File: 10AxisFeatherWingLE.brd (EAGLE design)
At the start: 50.8 x 22.9 mm, 26 parts, among them J5 QWIIC, U1 LSM9DS1, U2 BME280

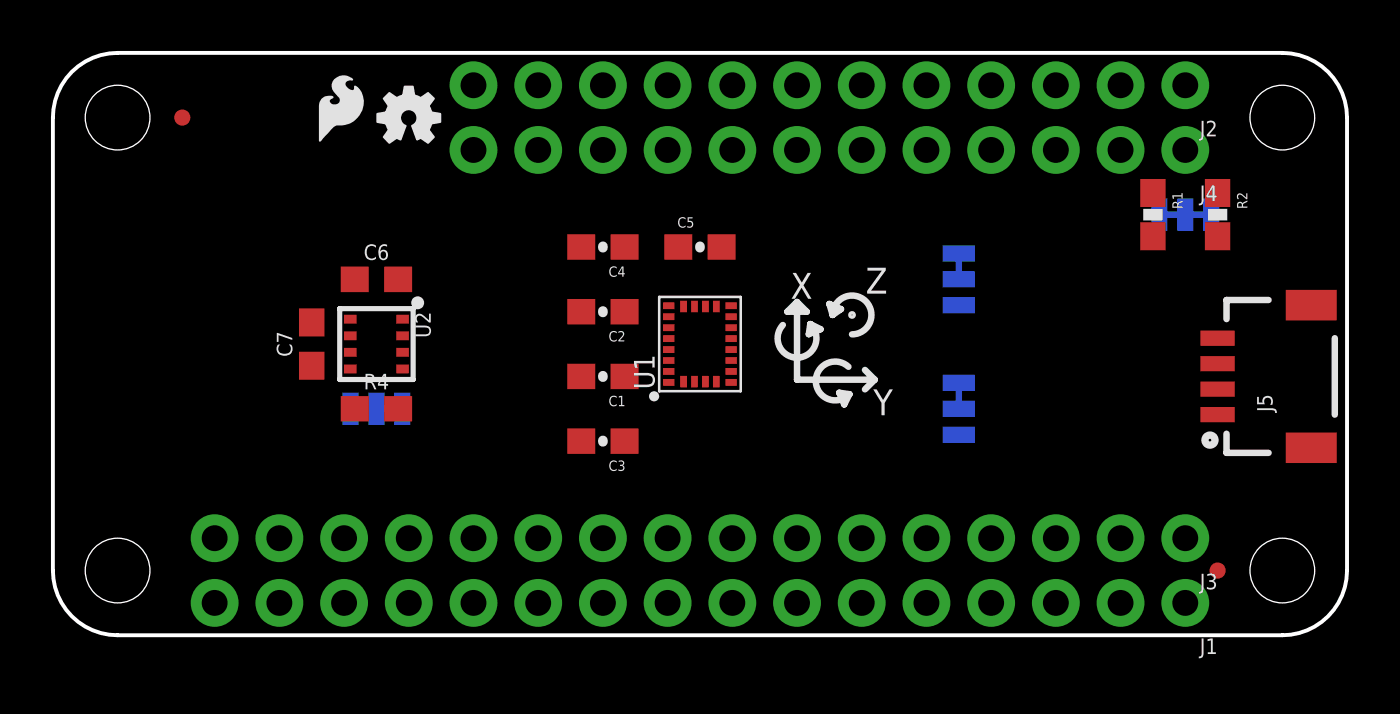
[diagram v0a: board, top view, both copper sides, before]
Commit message: Added traces
Added traces to board file.
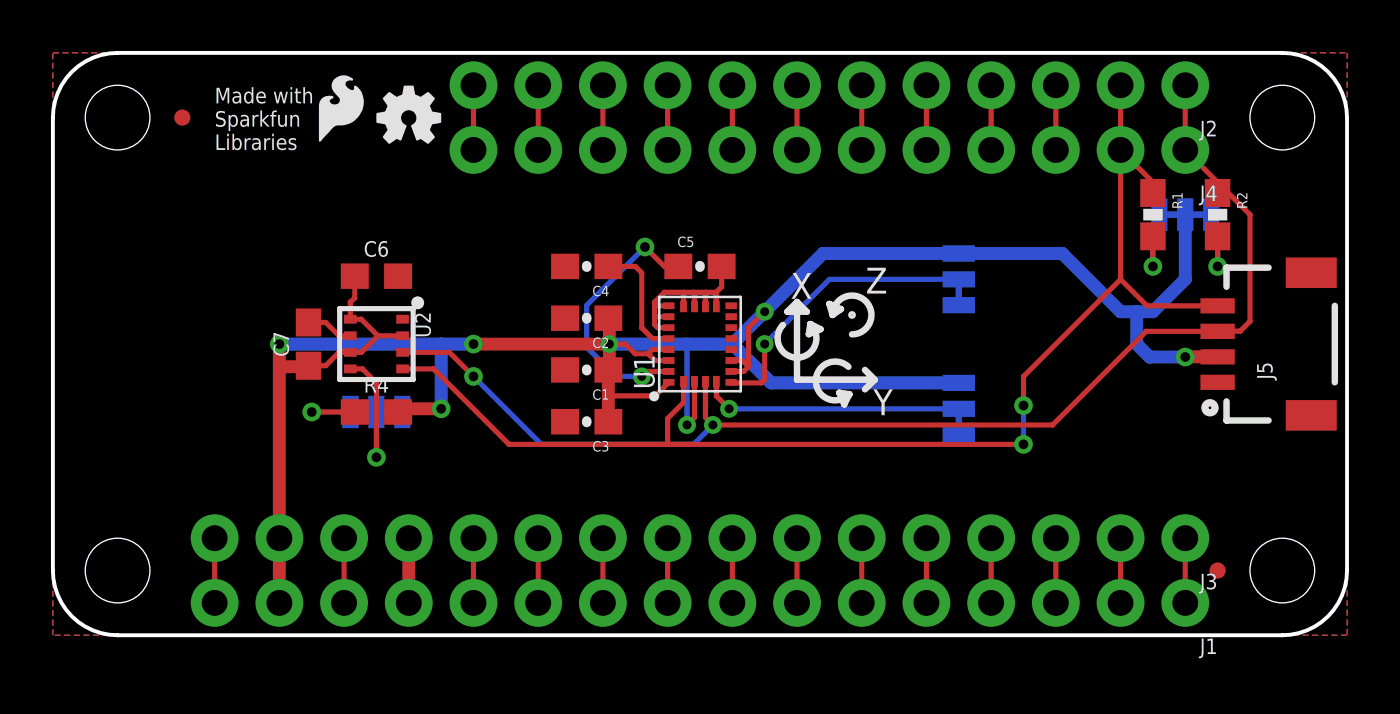
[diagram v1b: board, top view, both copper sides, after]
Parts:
- moved J5 1.27 mm to (45.7, 11.4)
- moved C4 0.99 mm to (21.0, 14.5)
- moved C3 0.99 mm to (21.0, 8.38)
- moved C5 0.76 mm to (25.4, 14.5)
- moved C1 0.68 mm to (21.0, 10.4)
- moved C2 0.68 mm to (21.0, 12.4)
- moved C7 0.13 mm to (10.0, 11.4)
- moved JP4 0.13 mm to (12.7, 8.76)
- moved R4 0.13 mm to (12.7, 8.76)
- moved C6 0.13 mm to (12.7, 14.1)
- turned JP2 to 270 degrees
- turned JP3 to 270 degrees
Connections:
- net SDO/ADR renamed SDO
- removed net SCK/SCL: U2.4
- removed net SDI/SDA: U2.3
- new net !RST: J1.16, J3.16
- new net A0: J1.12, J3.12
- new net A1: J1.11, J3.11
- new net A2: J1.10, J3.10
- new net A3: J1.9, J3.9
- new net A4: J1.8, J3.8
- new net A5: J1.7, J3.7
- new net AREF: J1.14, J3.14
- new net EN: J2.11, J4.11
- new net F0: J2.3, J4.3
- new net F1: J2.4, J4.4
- new net F2: J2.5, J4.5
- new net F3: J2.6, J4.6
- new net F4: J2.7, J4.7
- new net F5: J2.8, J4.8
- new net F6: J2.9, J4.9
- new net FREE: J1.1, J3.1
- new net MISO: J1.4, J3.4
- new net MOSI: J1.5, J3.5
- new net RX: J1.3, J3.3
- new net SCK: J1.6, J3.6
- new net TX: J1.2, J3.2
- new net VBAT: J2.12, J4.12
- new net VUSB: J2.10, J4.10
- net SCL: now also U2.4
- net SDA: now also U2.3
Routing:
- net VDD: track 0.00 -> 97.2 mm, vias 0 -> 7
- net SCL: track 0.00 -> 50.5 mm, vias 0 -> 2
- net SDA: track 0.00 -> 49.2 mm, vias 0 -> 2
- net GND: track 0.00 -> 13.0 mm
- net SDO_M: track 0.00 -> 11.0 mm, vias 0 -> 1
- net N$6: track 0.00 -> 10.3 mm, vias 0 -> 2
- net SDO_A/G: track 0.00 -> 9.88 mm, vias 0 -> 1
- net SDO: track 0.00 -> 5.95 mm, vias 0 -> 1
- net N$5: track 0.00 -> 4.81 mm
- net N$2: track 0.00 -> 3.32 mm, vias 0 -> 1
- net N$1: track 0.00 -> 3.32 mm, vias 0 -> 1
- net N$4: track 0.00 -> 3.21 mm, vias 0 -> 1
- net TX: track 0.00 -> 2.54 mm
- net SCK: track 0.00 -> 2.54 mm
- net RX: track 0.00 -> 2.54 mm
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- added copper zone on layer 1, net GND
- added copper zone on layer 16, net GND
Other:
- board text added: "Addr_A/G"
- board text added: "Addr_BME280"
- board text added: "Addr_Mag"
- board text added: "I2C Pull-up"
